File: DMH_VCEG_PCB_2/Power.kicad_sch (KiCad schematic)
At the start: 67 parts, among them J100 IDC_02x08, U1 TL074, U10 TL074, U11 TL074, U12 4001, U13 40106, U14 CD4066BE, U15 TL074, U16 4001, U17 TL074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

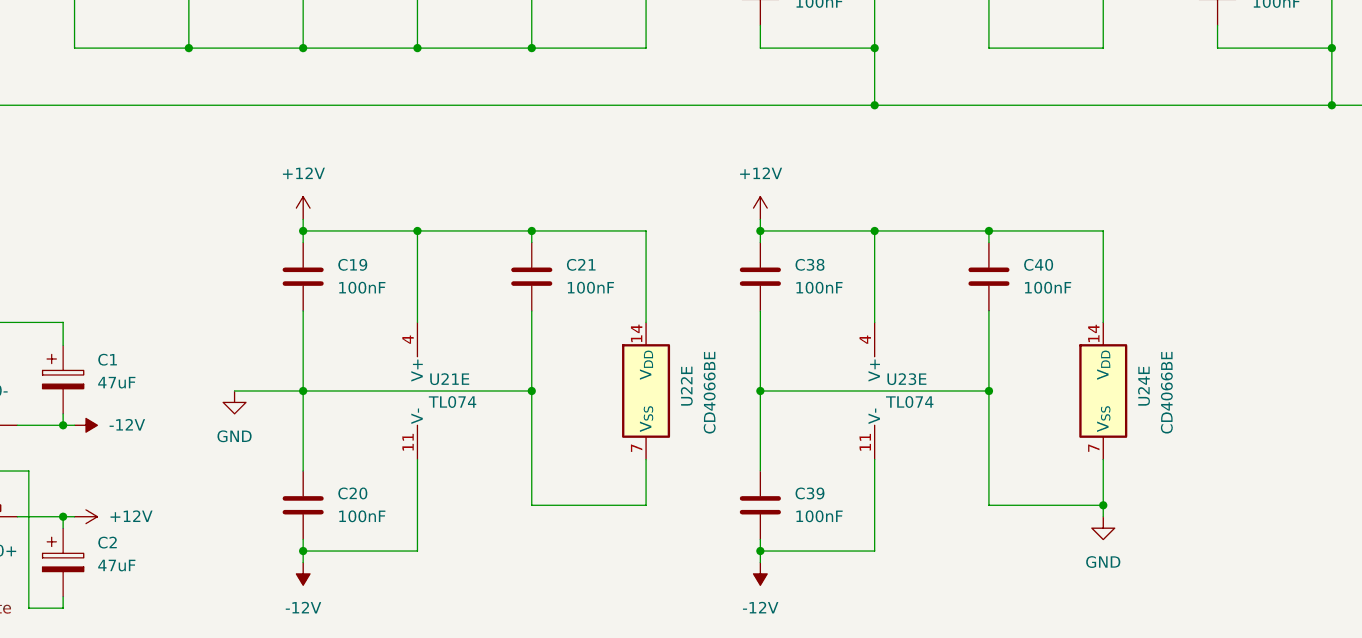
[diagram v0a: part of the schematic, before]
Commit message: Synced PCB 1 and 2
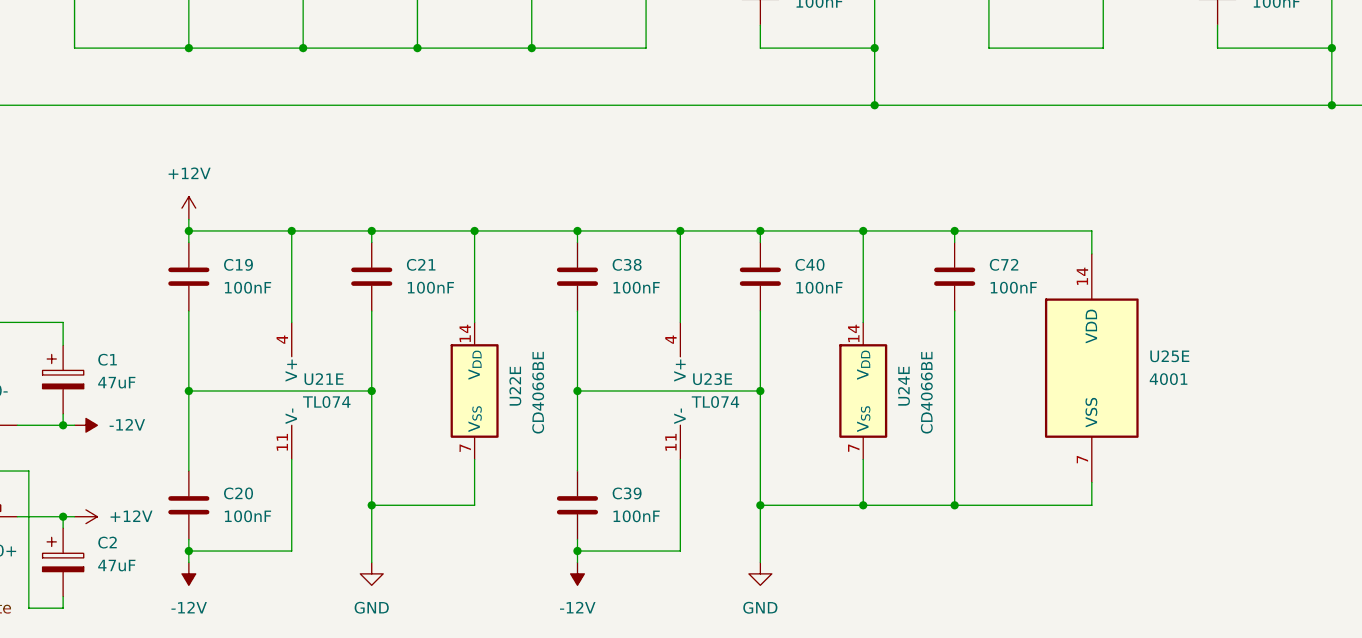
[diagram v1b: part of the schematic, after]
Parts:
- added C72: 100nF, Capacitor_THT:C_Disc_D4.3mm_W1.9mm_P5.00mm, symbol Device:C
- added U25: 4001, Package_DIP:DIP-14_W7.62mm_Socket, symbol 4xxx:4001
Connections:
- net +12V: now also C72.1, U25.14 (VDD)
- net GND: now also C72.2, U25.7 (VSS)
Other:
- moved on the sheet: C19, C20, C21, C38, C39, C40, U21E, U22E, U23E, U24E

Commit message: Restarted component placing on Main
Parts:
- added J23, J27: Conn_01x10_PinHeader, symbol SynthStuff:Conn_01x10_PinHeader
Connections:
- no-connect marks 4 -> 12

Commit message: PCB 2 Routing in progress
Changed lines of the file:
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@@
 		)
 	)
-	(text_box "ICs on PCB 1 (jacks):\nU1, U2, U3, U5, U6, U7\n\nICs on PCB 2 (pots):\nU4, U8, U9, U10, U21, U22"
+	(text_box "ICs on PCB 1 (jacks):\nU1, U2, U3, U5, U6, U7, U25\n\nICs on PCB 2 (pots):\nU4, U8, U9, U10, U21, U22"
 		(exclude_from_sim no)
 		(at 212.09 151.13 0)

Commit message: Reorganized repo
- Kicad 10
- Centralized and updated SynthStuff library
- Simulations folder
- Moved first version of PCB 1 to old_versions folder
- Gerbers folder
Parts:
- D1: value SB140- -> SB140; symbol SynthStuff:Power_Bus_Schotty_- -> Diode:SB140
- D2: value SB140+ -> SB140; symbol SynthStuff:Power_Bus_Schotty_+ -> Diode:SB140
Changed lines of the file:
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@@
 	)
 	(symbol
+		(lib_id "power:PWR_FLAG")
+		(at 49.53 185.42 0)
+		(unit 1)
+		(body_style 1)
+		(exclude_from_sim no)
+		(in_bom yes)
+		(on_board yes)
+		(in_pos_files yes)
+		(dnp no)
+		(fields_autoplaced yes)
+		(property "Reference" "#FLG01"
+			(at 49.53 183.515 0)
+			(hide yes)
+			(show_name no)
+			(do_not_autoplace no)
+			(effects
+				(font
+					(size 1.27 1.27)
+				)
+			)
+		)
+		(property "Value" "PWR_FLAG"
+			(at 49.53 180.34 0)
+			(show_name no)
+			(do_not_autoplace no)
+			(effects
+				(font
+					(size 1.27 1.27)
+				)
+			)
+		)
+		(property "Footprint" ""
+			(at 49.53 185.42 0)
+			(hide yes)
+			(show_name no)
+			(do_not_autoplace no)
+			(effects
+				(font
+					(size 1.27 1.27)
+				)
+			)
+		)
+		(property "Datasheet" ""
+			(at 49.53 185.42 0)
+			(hide yes)
+			(show_name no)
+			(do_not_autoplace no)
+			(effects
+				(font
+					(size 1.27 1.27)
+				)
+			)
+		)
+		(property "Description" "Special symbol for telling ERC where power comes from"
+			(at 49.53 185.42 0)
+			(hide yes)
+			(show_name no)
+			(do_not_autoplace no)
+			(effects
+				(font
+					(size 1.27 1.27)
+				)
+			)
+		)
+		(pin "1"
+		)
+		(instances
+			(project "DMH_VCEG_PCB_2"
+				(path "/58f4306d-5387-4983-bb08-41a2313fd315/0cdf34b2-39cd-4d9e-981a-97cd34791509"
+					(reference "#FLG01")
+					(unit 1)
+				)
+			)
+		)
+	)
+	(symbol
 		(lib_id "power:+12V")
 		(at 63.5 152.4 0)
@@
 	)
 	(symbol
+		(lib_id "power:PWR_FLAG")
+		(at 49.53 175.26 180)
+		(unit 1)
+		(body_style 1)
+		(exclude_from_sim no)
+		(in_bom yes)
+		(on_board yes)
+		(in_pos_files yes)
+		(dnp no)
+		(fields_autoplaced yes)
+		(property "Reference" "#FLG02"
+			(at 49.53 177.165 0)
+			(hide yes)
+			(show_name no)
+			(do_not_autoplace no)
+			(effects
+				(font
+					(size 1.27 1.27)
+				)
+			)
+		)
+		(property "Value" "PWR_FLAG"
+			(at 49.53 180.34 0)
+			(show_name no)
+			(do_not_autoplace no)
+			(effects
+				(font
+					(size 1.27 1.27)
+				)
+			)
+		)
+		(property "Footprint" ""
+			(at 49.53 175.26 0)
+			(hide yes)
+			(show_name no)
+			(do_not_autoplace no)
+			(effects
+				(font
+					(size 1.27 1.27)
+				)
+			)
+		)
+		(property "Datasheet" ""
+			(at 49.53 175.26 0)
+			(hide yes)
+			(show_name no)
+			(do_not_autoplace no)
+			(effects
+				(font
+					(size 1.27 1.27)
+				)
+			)
+		)
+		(property "Description" "Special symbol for telling ERC where power comes from"
+			(at 49.53 175.26 0)
+			(hide yes)
+			(show_name no)
+			(do_not_autoplace no)
+			(effects
+				(font
+					(size 1.27 1.27)
+				)
+			)
+		)
+		(pin "1"
+		)
+		(instances
+			(project "DMH_VCEG_PCB_2"
+				(path "/58f4306d-5387-4983-bb08-41a2313fd315/0cdf34b2-39cd-4d9e-981a-97cd34791509"
+					(reference "#FLG02")
+					(unit 1)
+				)
+			)
+		)
+	)
+	(symbol
 		(lib_id "power:-12V")
 		(at 106.68 190.5 180)
@@
 	)
 	(symbol
-		(lib_id "SynthStuff:Power_Bus_Schotty_-")
+		(lib_id "Diode:SB140")
 		(at 40.64 175.26 0)
 		(unit 1)
@@
 			)
 		)
-		(property "Value" "SB140-"
+		(property "Value" "SB140"
 			(at 40.3225 171.45 0)
 			(show_name no)
@@
 	)
 	(symbol
-		(lib_id "SynthStuff:Power_Bus_Schotty_+")
+		(lib_id "Diode:SB140")
 		(at 40.64 185.42 0)
 		(mirror y)
@@
 			)
 		)
-		(property "Value" "SB140+"
-			(at 40.9575 189.23 0)
+		(property "Value" "SB140"
+			(at 40.64 189.23 0)
 			(show_name no)
 			(do_not_autoplace no)
